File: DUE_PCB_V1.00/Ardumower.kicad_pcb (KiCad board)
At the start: 2 copper layers, 169.4 x 95.9 mm, 73 parts, among them J1 9V IN, J10 Sonar_R, J11 Sonar_C, J12 Sonar_L, J13 P_Right, J15 Button, J16 Button, J17 Button, J18 Button, J19 P_Left, J2 I2C0_1, J20 Remote, J21 PCB_2, J22 3.3V, J23 GND, J24 RX & TX, J25 5V IN, J26 Motor Left, J27 Cutter Motor, J28 Motor Right, J29 3.3V IN, J3 I2C0_2, J30 I2C1_2, J4 I2C1_1, J5 Bumper, J6 Drop_Left, J7 Drop_Right, J8 Tilt, J9 Rain, U1 MC33926, U2 MC33926

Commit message: Remove 2x4 Motor Pin Connectors
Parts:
- removed D6: LED_Red, LED_THT:LED_D3.0mm
- removed J26: Motor Left, Connector_PinSocket_2.54mm:PinSocket_2x04_P2.54mm_Vertical
- removed J27: Cutter Motor, Connector_PinSocket_2.54mm:PinSocket_2x04_P2.54mm_Vertical
- removed J28: Motor Right, Connector_PinSocket_2.54mm:PinSocket_2x04_P2.54mm_Vertical
- removed JP4, JP5, JP6: 5V, Connector_PinSocket_2.54mm:PinSocket_1x02_P2.54mm_Vertical
- removed R14, R15: 100, Resistor_THT:R_Axial_DIN0207_L6.3mm_D2.5mm_P2.54mm_Vertical
- removed R17, R19, R21, R23, R25, R27: 1.5KO, Resistor_THT:R_Axial_DIN0207_L6.3mm_D2.5mm_P2.54mm_Vertical
- removed R18, R20, R22, R24, R26, R28: 1KO, Resistor_THT:R_Axial_DIN0207_L6.3mm_D2.5mm_P2.54mm_Vertical
- added H1: MountingHole_Pad, MountingHole:MountingHole_2.2mm_M2_Pad_TopBottom, F.Cu at (41.8, 38.4)
- added H2: MountingHole_Pad, MountingHole:MountingHole_2.2mm_M2_Pad_TopBottom, F.Cu at (205.8, 38.3)
- added H3: MountingHole_Pad, MountingHole:MountingHole_2.2mm_M2_Pad_TopBottom, F.Cu at (205.6, 128.2)
- added H4: MountingHole_Pad, MountingHole:MountingHole_2.2mm_M2_Pad_TopBottom, F.Cu at (41.9, 128.4)
- added J14: Buzzer, Connector_PinHeader_2.54mm:PinHeader_1x03_P2.54mm_Vertical, F.Cu at (53.5, 120.9)
- added J31: Ser3, Connector_PinHeader_2.54mm:PinHeader_1x05_P2.54mm_Vertical, F.Cu at (162.7, 40.3)
- added J32: 24V In, TerminalBlock:TerminalBlock_bornier-2_P5.08mm, F.Cu at (202.5, 85.3)
- D5: value LED_Green -> 1N5819; footprint LED_THT:LED_D3.0mm -> Diode_THT:D_DO-41_SOD81_P10.16mm_Horizontal
- J15: footprint Zimprich:Pin_Header_KK110_1x02_3D -> Connector_PinHeader_2.54mm:PinHeader_1x02_P2.54mm_Vertical
- J16: value Button -> US1; footprint Zimprich:Pin_Header_KK110_1x02_3D -> Connector_PinHeader_2.54mm:PinHeader_1x02_P2.54mm_Vertical
- J17: value Button -> US2; footprint Zimprich:Pin_Header_KK110_1x02_3D -> Connector_PinHeader_2.54mm:PinHeader_1x02_P2.54mm_Vertical
- J18: value Button -> US3; footprint Zimprich:Pin_Header_KK110_1x02_3D -> Connector_PinHeader_2.54mm:PinHeader_1x02_P2.54mm_Vertical
- J22: value 3.3V -> Ser0; footprint Connector_PinHeader_2.54mm:PinHeader_1x04_P2.54mm_Vertical -> Connector_PinHeader_2.54mm:PinHeader_1x05_P2.54mm_Vertical
- J23: value GND -> Ser1; footprint Connector_PinHeader_2.54mm:PinHeader_1x04_P2.54mm_Vertical -> Connector_PinHeader_2.54mm:PinHeader_1x05_P2.54mm_Vertical
- J24: value RX & TX -> Ser2; footprint Connector_PinHeader_2.54mm:PinHeader_1x04_P2.54mm_Vertical -> Connector_PinHeader_2.54mm:PinHeader_1x05_P2.54mm_Vertical
- moved D5 124.6 mm to (192.4, 87.5), turned to 90 degrees
- moved J7 108.6 mm to (163.3, 114.8)
- moved J6 108.5 mm to (155.3, 114.8)
- moved J22 95.5 mm to (148.8, 40.3)
- moved J24 95.4 mm to (158.1, 40.3)
- moved J23 95.3 mm to (153.4, 40.3)
- moved JP3 58.0 mm to (58.9, 70.3)
- moved J30 55.5 mm to (106.2, 40.3)
- moved D8 54.2 mm to (53.7, 70.2), turned to 270 degrees
- moved R1 53.6 mm to (94.4, 47.7)
- moved R2 52.3 mm to (110.2, 47.8)
- moved R4 46.9 mm to (110.2, 40.2)
- moved D7 45.4 mm to (53.7, 57.0), turned to 270 degrees
- moved JP1 45.4 mm to (58.9, 58.2)
- moved J29 43.6 mm to (45.0, 69.5), turned to 270 degrees
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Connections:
- D5 pad 1: GND -> +24V
- J22 pad 1: +3V3 -> +5V
- J22 pad 2: +3V3 -> TX0
- J22 pad 3: +3V3 -> RX0
- J23 pad 1: GND -> +5V
- J23 pad 2: GND -> TX1
- J23 pad 3: GND -> RX1
- J23 pad 4: GND -> +3V3
- J24 pad 1: TX1 -> +5V
- J24 pad 2: RX1 -> TX2
- J24 pad 3: TX2 -> RX2
- J24 pad 4: RX2 -> +3V3
- XA1 pad A11: pinMotorMowRpm -> (no net)
- XA1 pad CANR: pinOdometryRight -> (no net)
- XA1 pad D0: (no net) -> RX0
- XA1 pad D1: (no net) -> TX0
- XA1 pad D14: (no net) -> RX3
- XA1 pad D15: (no net) -> TX3
- XA1 pad D6: pinGreenLED -> (no net)
- XA1 pad D7: pinRedLED -> (no net)
- XA1 pad DAC0: pinOdometryLeft -> (no net)
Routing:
- net GND: track 798.0 -> 0.00 mm
- net +5V: track 295.6 -> 0.00 mm, vias 1 -> 0
- net +3V3: track 204.0 -> 0.00 mm
- net pinDropRight: track 172.0 -> 0.00 mm, vias 1 -> 0
- net IOREV: track 172.0 -> 0.00 mm, vias 2 -> 0
- net pinMotorLeftPWM: track 156.7 -> 0.00 mm, vias 1 -> 0
- net pinMotorLeftDir: track 139.9 -> 0.00 mm, vias 1 -> 0
- net pinDropLeft: track 136.3 -> 0.00 mm, vias 1 -> 0
- net pinRemoteSwitch: track 128.9 -> 0.00 mm
- net pinChargeRelay: track 122.9 -> 0.00 mm, vias 1 -> 0
- net pinMotorMowSense: track 119.8 -> 0.00 mm
- net pinOdometryLeft: track 117.9 -> 0.00 mm, vias 1 -> 0
- net pinChargeVoltage: track 114.0 -> 0.00 mm, vias 1 -> 0
- net pinChargeCurrent: track 109.6 -> 0.00 mm, vias 1 -> 0
- net pinBuzzer: track 107.1 -> 0.00 mm
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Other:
- board size 169.4 x 95.9 mm -> 169.4 x 95.6 mm
- board text removed: "GND"
- board text removed: "RX2"
- board text removed: "TX1"
- board text removed: "TX2"

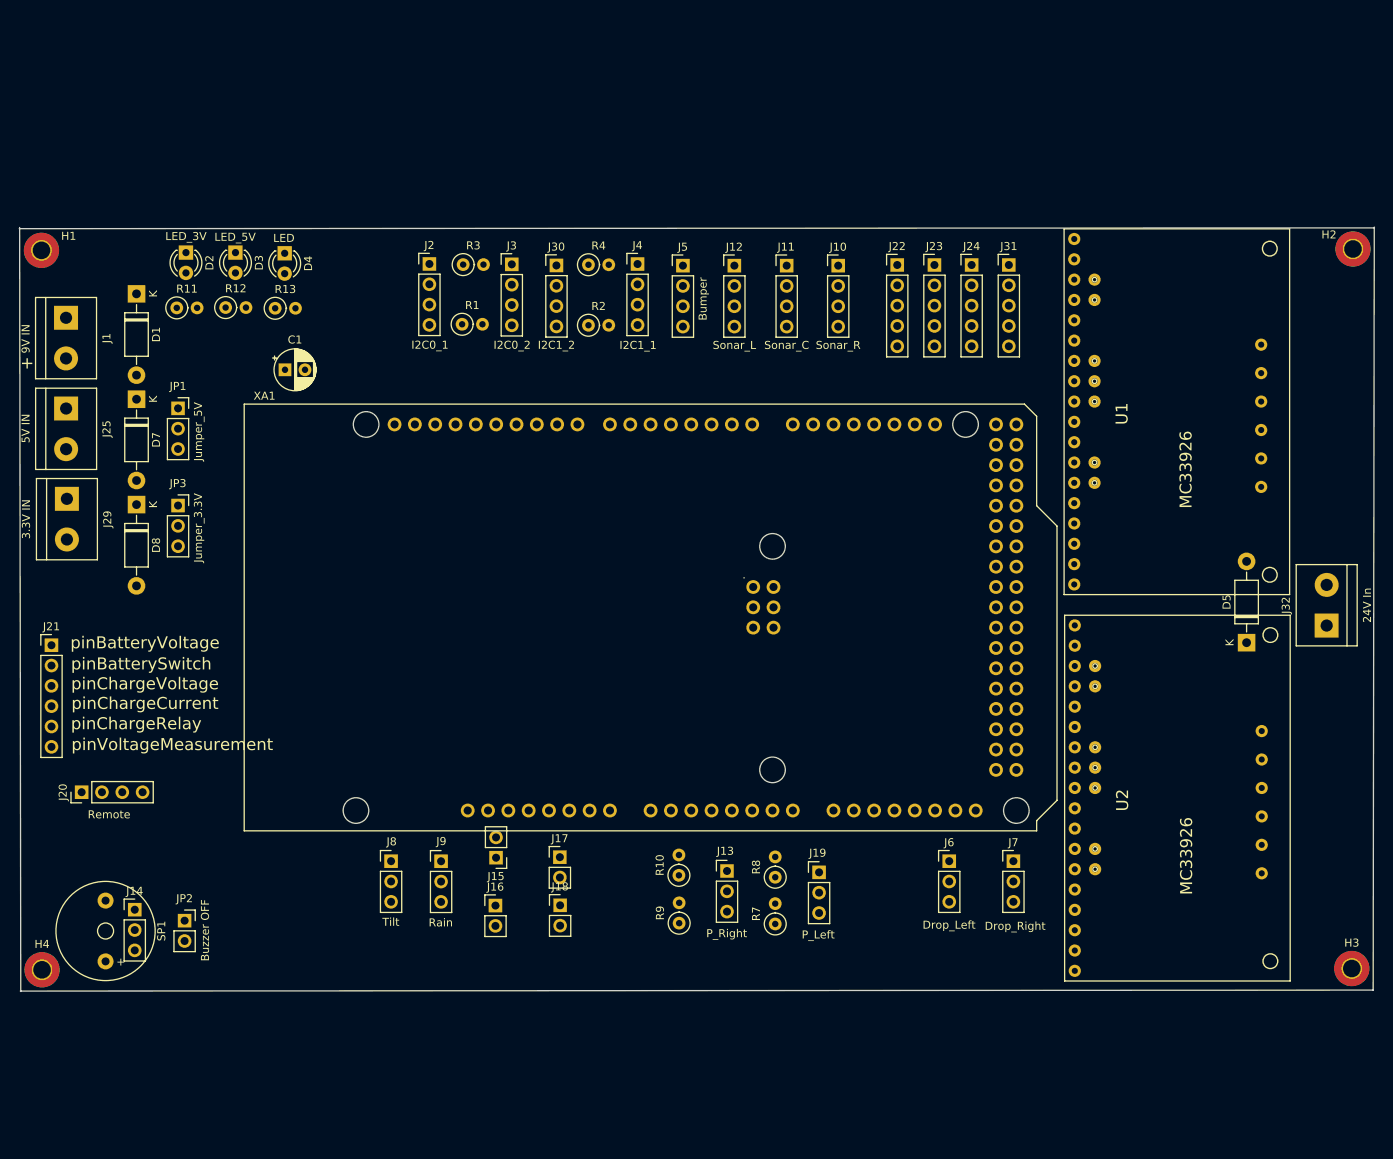
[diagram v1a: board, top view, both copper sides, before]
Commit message: Sort Connectors on PCB
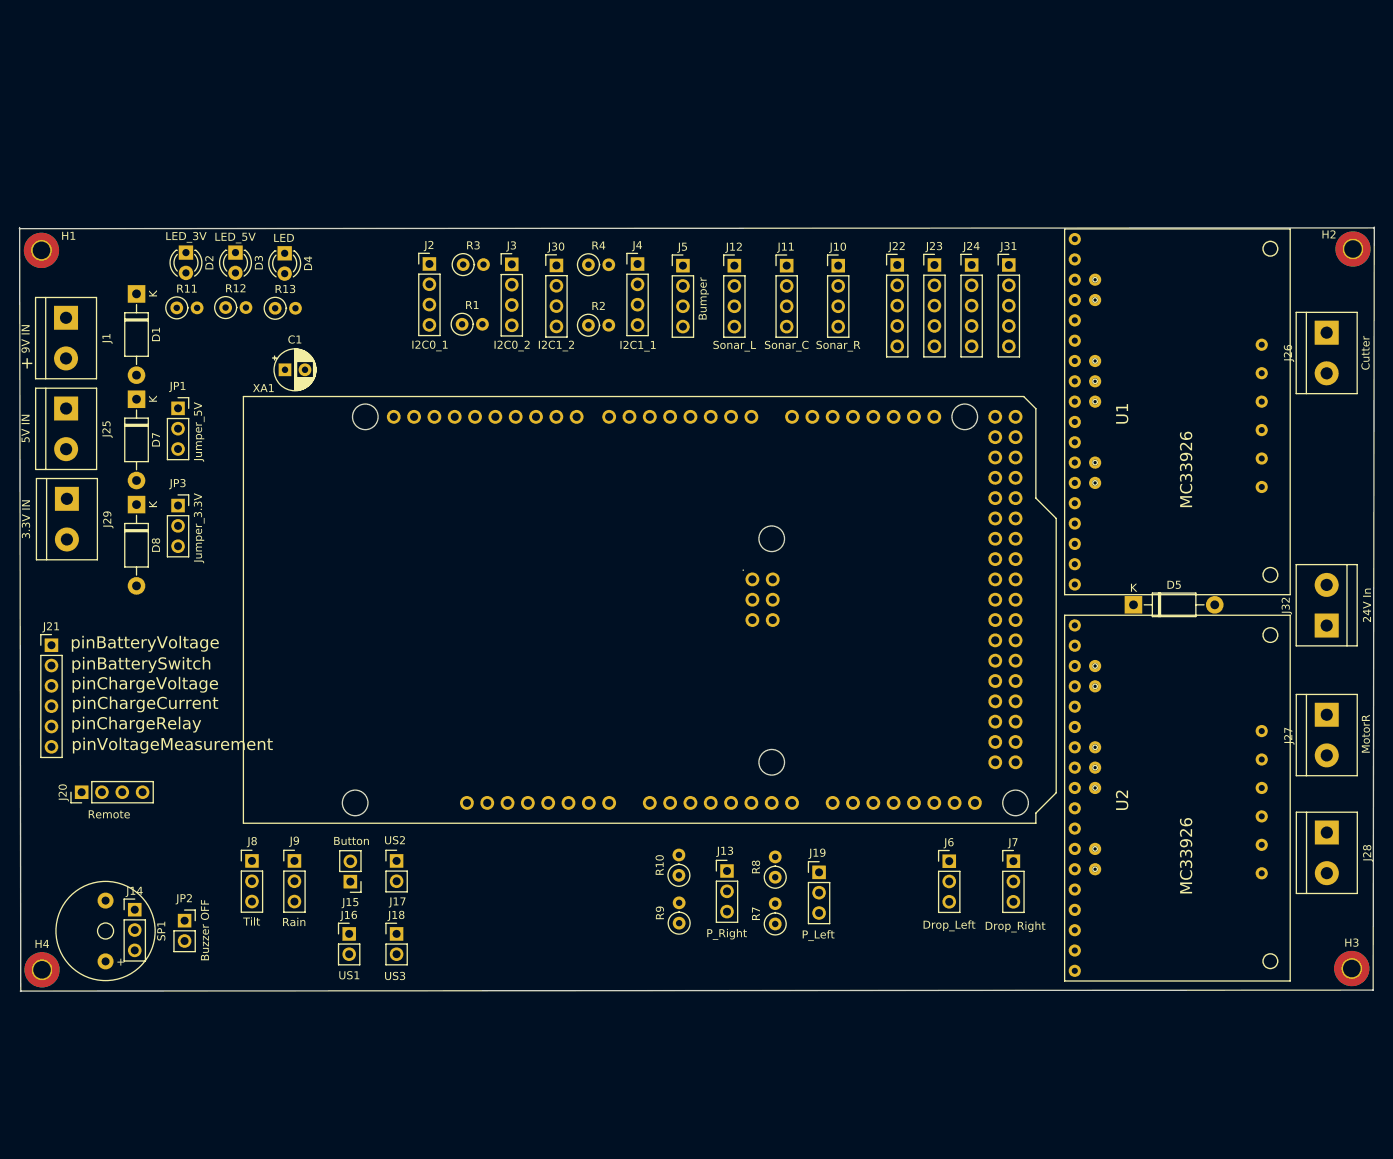
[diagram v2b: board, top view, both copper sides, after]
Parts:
- added J26: Cutter, TerminalBlock:TerminalBlock_bornier-2_P5.08mm, F.Cu at (202.5, 48.7)
- added J27: MotorR, TerminalBlock:TerminalBlock_bornier-2_P5.08mm, F.Cu at (202.5, 96.5)
- added J28: MotorL, TerminalBlock:TerminalBlock_bornier-2_P5.08mm, F.Cu at (202.5, 111.2)
- moved J18 20.7 mm to (86.2, 123.9)
- moved J17 20.4 mm to (86.2, 114.8)
- moved J16 18.6 mm to (80.3, 123.9)
- moved J15 18.5 mm to (80.4, 117.3)
- moved J9 18.3 mm to (73.4, 114.8)
- moved J8 17.4 mm to (68.1, 114.8)
- moved D5 14.9 mm to (178.3, 82.8), turned to 0 degrees
- moved XA1 0.96 mm to (67.0, 110.0)
- moved U1 0.07 mm to (208.8, 85.3)
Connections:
- U1 pad 23: (no net) -> Net-(J26-Pad2)
- U1 pad 24: (no net) -> Net-(J26-Pad1)
- U2 pad 19: (no net) -> Net-(J28-Pad2)
- U2 pad 20: (no net) -> Net-(J28-Pad1)
- U2 pad 23: (no net) -> Net-(J27-Pad2)
- U2 pad 24: (no net) -> Net-(J27-Pad1)

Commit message: Add Pin Description on PCB
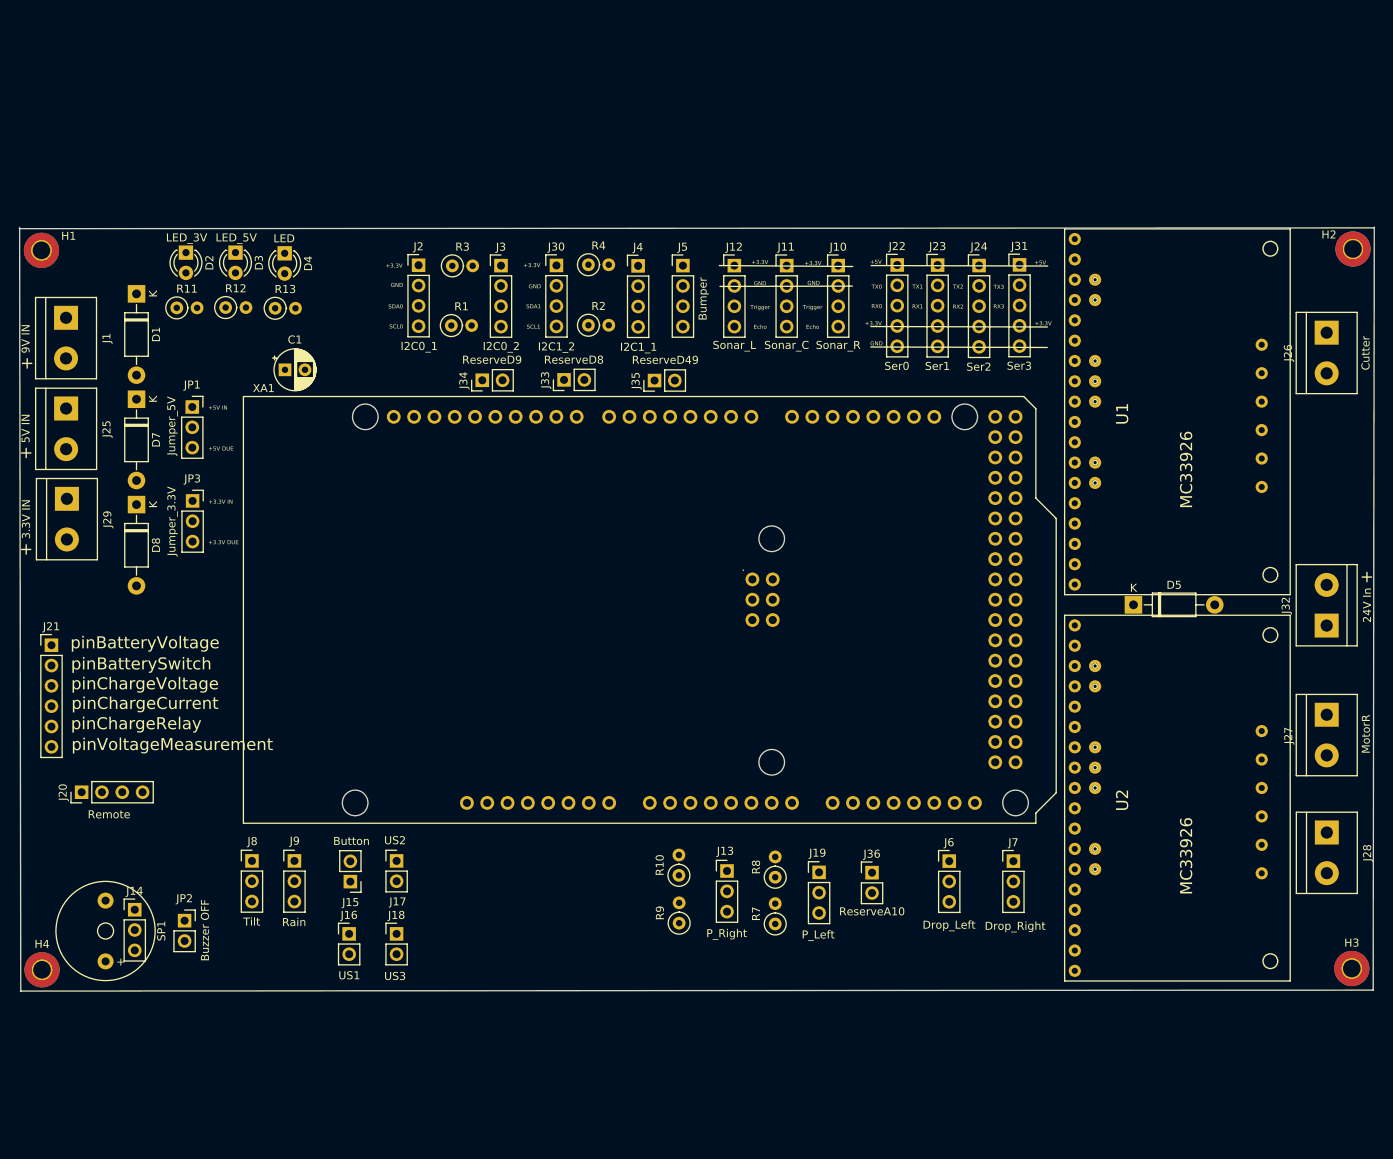
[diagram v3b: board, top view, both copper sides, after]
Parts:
- added J33: ReserveD8, Connector_PinHeader_2.54mm:PinHeader_1x02_P2.54mm_Vertical, F.Cu at (107.1, 54.6)
- added J34: ReserveD9, Connector_PinHeader_2.54mm:PinHeader_1x02_P2.54mm_Vertical, F.Cu at (96.9, 54.7)
- added J35: ReserveD49, Connector_PinHeader_2.54mm:PinHeader_1x02_P2.54mm_Vertical, F.Cu at (118.4, 54.7)
- added J36: ReserveA10, Connector_PinHeader_2.54mm:PinHeader_1x02_P2.54mm_Vertical, F.Cu at (145.6, 116.2)
- moved JP3 1.91 mm to (60.7, 69.8)
- moved JP1 1.79 mm to (60.7, 58.0)
- moved J3 1.36 mm to (99.2, 40.4)
- moved R1 1.36 mm to (93.0, 47.8)
- moved R3 1.36 mm to (93.2, 40.4)
- moved J2 1.36 mm to (89.0, 40.3)
- moved J31 1.34 mm to (164.1, 40.2)
- moved J24 0.93 mm to (159.0, 40.3)
- moved J23 0.40 mm to (153.8, 40.3)
- moved J4 0.24 mm to (116.4, 40.4)
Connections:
- XA1 pad A10: (no net) -> pinReserveA10
- XA1 pad D49: (no net) -> pinReserveD49
- XA1 pad D8: (no net) -> pinReserveD8
- XA1 pad D9: (no net) -> pinReserveD9
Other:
- board text added: "+3.3V"
- board text added: "+3.3V DUE"
- board text added: "+3.3V IN"
- board text added: "+5V"
- board text added: "+5V DUE"
- board text added: "+5V IN"
- board text added: "Echo"
- board text added: "GND"
- board text added: "RX0"
- board text added: "RX1"
- board text added: "RX2"
- board text added: "RX3"
- board text added: "SCL0"
- board text added: "SCL1"
- board text added: "SDA0"
- board text added: "SDA1"
- board text added: "TX0"
- board text added: "TX1"
- board text added: "TX2"
- board text added: "TX3"
- board text added: "Trigger"

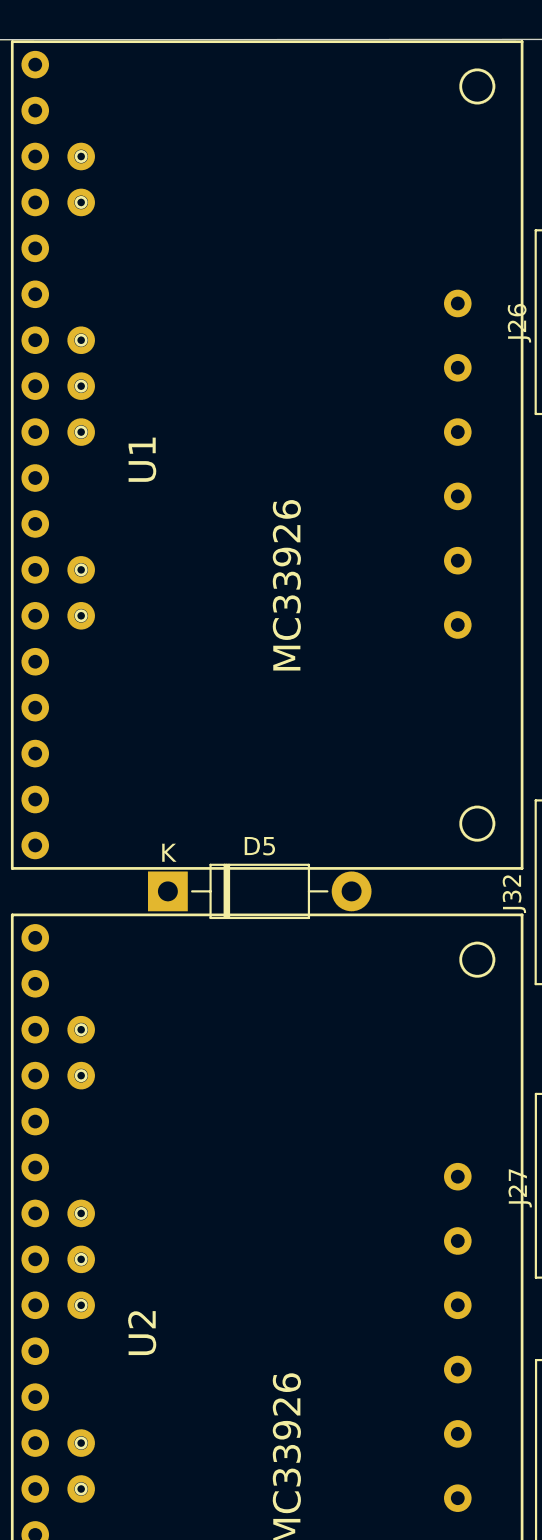
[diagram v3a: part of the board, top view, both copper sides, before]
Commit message: Add Zener Diode
3.3 V zener diode to clamp the current sense output voltage to a maximum of ~3.3 V
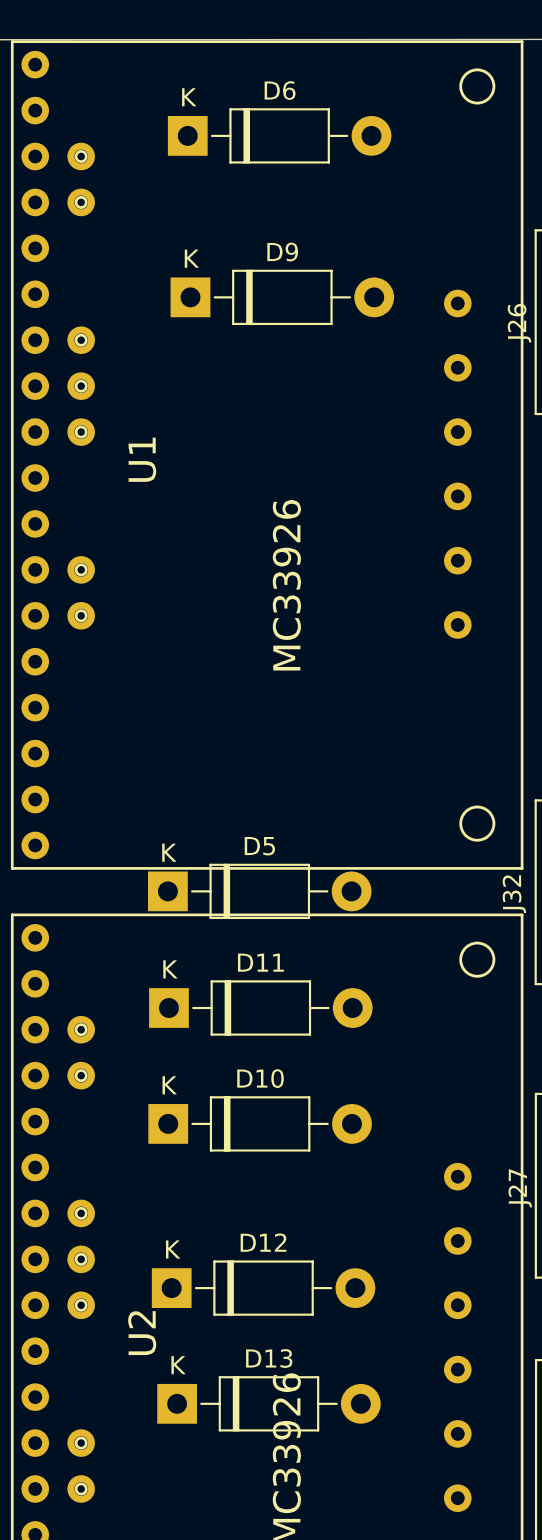
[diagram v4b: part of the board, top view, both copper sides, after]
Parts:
- added D10: 1N4728A, Diode_THT:D_DO-41_SOD81_P10.16mm_Horizontal, F.Cu at (178.3, 95.6)
- added D11: 1N4728A, Diode_THT:D_DO-41_SOD81_P10.16mm_Horizontal, F.Cu at (178.4, 89.2)
- added D12: 1N4728A, Diode_THT:D_DO-41_SOD81_P10.16mm_Horizontal, F.Cu at (178.5, 104.7)
- added D13: 1N4728A, Diode_THT:D_DO-41_SOD81_P10.16mm_Horizontal, F.Cu at (178.8, 111.1)
- added D6: 1N4728A, Diode_THT:D_DO-41_SOD81_P10.16mm_Horizontal, F.Cu at (179.4, 41.0)
- added D9: 1N4728A, Diode_THT:D_DO-41_SOD81_P10.16mm_Horizontal, F.Cu at (179.6, 49.9)
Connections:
- U1 pad 17: pinMotorMowFault -> Net-(D9-Pad2)
- U1 pad 18: pinMotorMowSense -> Net-(D6-Pad2)
- U1 pad 8: pinMotorMowFault -> Net-(D9-Pad2)
- U2 pad 17: pinMotorRightFault -> Net-(D11-Pad2)
- U2 pad 18: pinMotorRightSense -> Net-(D10-Pad2)
- U2 pad 8: pinMotorLeftFault -> Net-(D13-Pad2)
- U2 pad 9: pinMotorLeftSense -> Net-(D12-Pad2)
